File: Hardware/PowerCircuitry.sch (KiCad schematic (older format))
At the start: 32 parts, among them J4 Conn_01x02_Male, J5 Conn_01x02_Male, Q5 MMBT3904, Q6 MMBT3904, SW3 SW_SPST

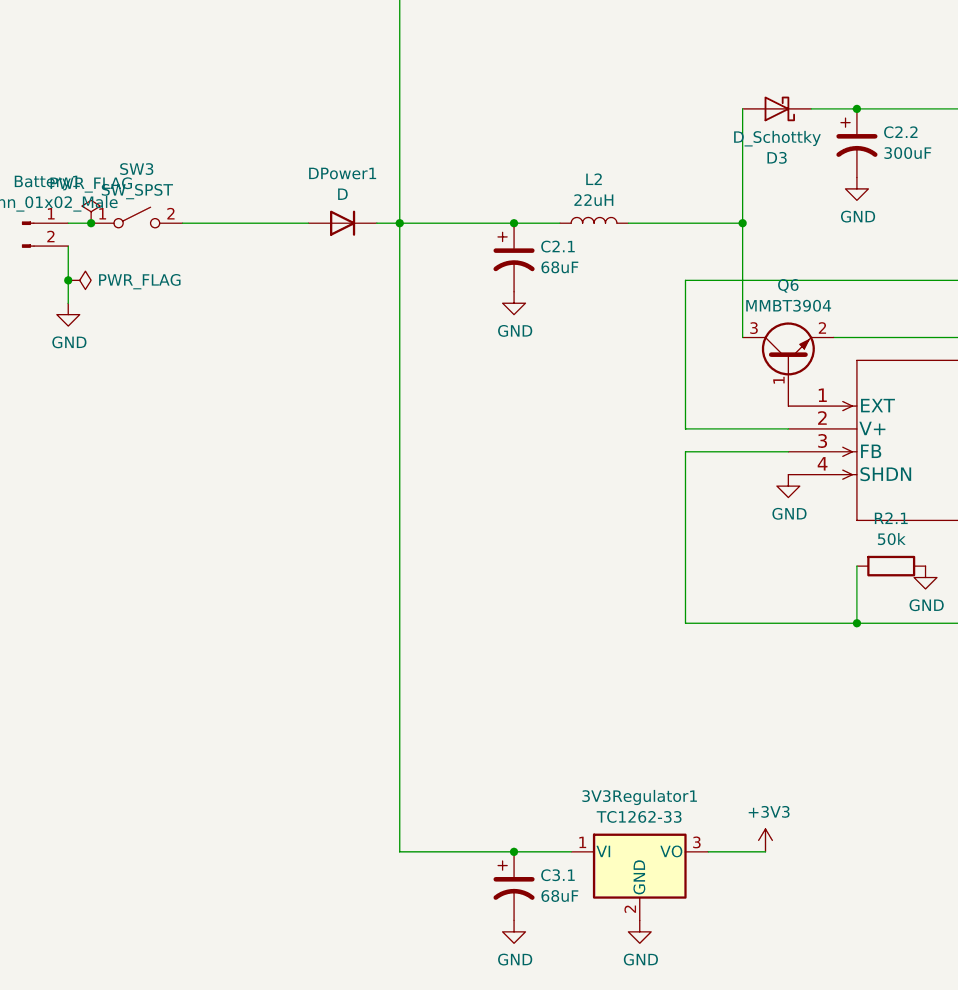
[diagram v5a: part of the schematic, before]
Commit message: Genuine Confusion
Changed to an ideal diode whatever tf that is
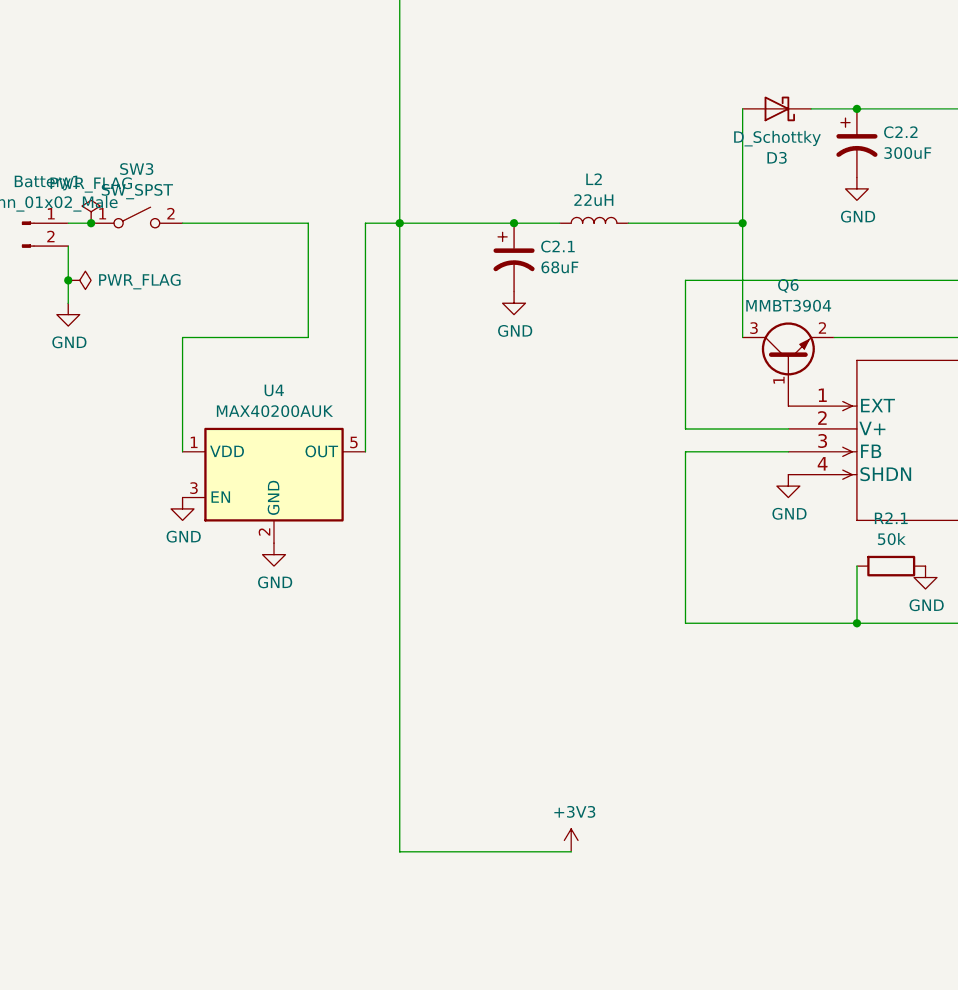
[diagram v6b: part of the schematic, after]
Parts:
- removed 3V3Regulator1: TC1262-33, Package_TO_SOT_SMD:SOT-223-3_TabPin2, symbol Regulator_Linear:TC1262-33
- removed C3.1: 68uF, Capacitor_SMD:C_0603_1608Metric, symbol Device:CP1
- removed DPower1: D, Diode_SMD:D_0603_1608Metric, symbol Device:D
- added U4: MAX40200AUK, Package_TO_SOT_SMD:SOT-23-5, symbol Analog_Switch:MAX40200AUK
- SW3: footprint Button_Switch_SMD:SW_DIP_SPSTx01_Slide_6.7x4.1mm_W6.73mm_P2.54mm_LowProfile_JPin -> Button_Switch_SMD:SW_DIP_SPSTx01_Slide_9.78x4.72mm_W8.61mm_P2.54mm
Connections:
- net +3V3: now also C1.1.1, C2.1.1, L1.1, L2.1, U4.5 (OUT)
- net GND: now also U4.2 (GND), U4.3 (EN)
- net at SW3.2 (B): now also U4.1 (VDD)
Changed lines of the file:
@@
 EESchema Schematic File Version 4
+LIBS:VLAD-cache
 EELAYER 30 0
 EELAYER END
@@
 	1000 4100 1000 4000
 $Comp
-L Regulator_Linear:TC1262-33 3V3Regulator1
-U 1 1 60725034
-P 3500 6500
-F 0 "3V3Regulator1" H 3500 6742 50  0000 C CNN
-F 1 "TC1262-33" H 3500 6651 50  0000 C CNN
-F 2 "Package_TO_SOT_SMD:SOT-223-3_TabPin2" H 3500 6725 50  0001 C CIN
-F 3 "http://ww1.microchip.com/downloads/en/DeviceDoc/21373C.pdf" H 3500 6200 50  0001 C CNN
-	1    3500 6500
-	1    0    0    -1
-$EndComp
-$Comp
 L power:+3V3 #PWR041
 U 1 1 6072852F
-P 4050 6500
-F 0 "#PWR041" H 4050 6350 50  0001 C CNN
-F 1 "+3V3" H 4065 6673 50  0000 C CNN
-F 2 "" H 4050 6500 50  0001 C CNN
-F 3 "" H 4050 6500 50  0001 C CNN
-	1    4050 6500
-	1    0    0    -1
-$EndComp
-$Comp
-L power:GND #PWR039
-U 1 1 60725C54
-P 3500 6800
-F 0 "#PWR039" H 3500 6550 50  0001 C CNN
-F 1 "GND" H 3505 6627 50  0000 C CNN
-F 2 "" H 3500 6800 50  0001 C CNN
-F 3 "" H 3500 6800 50  0001 C CNN
-	1    3500 6800
+P 3200 6500
+F 0 "#PWR041" H 3200 6350 50  0001 C CNN
+F 1 "+3V3" H 3215 6673 50  0000 C CNN
+F 2 "" H 3200 6500 50  0001 C CNN
+F 3 "" H 3200 6500 50  0001 C CNN
+	1    3200 6500
 	1    0    0    -1
 $EndComp
@@
 Wire Wire Line
 	4450 5500 3700 5500
-Wire Wire Line
-	3800 6500 4050 6500
 Connection ~ 2950 3750
 Wire Wire Line
@@
 	6550 5150 6950 5150
 Connection ~ 6950 5150
-Wire Wire Line
-	2350 3750 2450 3750
-$Comp
-L Device:CP1 C3.1
-U 1 1 607BC104
-P 2950 6650
-F 0 "C3.1" H 3065 6696 50  0000 L CNN
-F 1 "68uF" H 3065 6605 50  0000 L CNN
-F 2 "Capacitor_SMD:C_0603_1608Metric" H 2950 6650 50  0001 C CNN
-F 3 "~" H 2950 6650 50  0001 C CNN
-	1    2950 6650
-	1    0    0    -1
-$EndComp
-Wire Wire Line
-	2950 6500 3200 6500
-$Comp
-L power:GND #PWR038
-U 1 1 607BD21C
-P 2950 6800
-F 0 "#PWR038" H 2950 6550 50  0001 C CNN
-F 1 "GND" H 2955 6627 50  0000 C CNN
-F 2 "" H 2950 6800 50  0001 C CNN
-F 3 "" H 2950 6800 50  0001 C CNN
-	1    2950 6800
-	1    0    0    -1
-$EndComp
-Wire Wire Line
-	2450 6500 2950 6500
-Connection ~ 2950 6500
-$Comp
-L Device:D DPower1
-U 1 1 607B8542
-P 2200 3750
-F 0 "DPower1" H 2200 3534 50  0000 C CNN
-F 1 "D" H 2200 3625 50  0000 C CNN
-F 2 "Diode_SMD:D_0603_1608Metric" H 2200 3750 50  0001 C CNN
-F 3 "~" H 2200 3750 50  0001 C CNN
-	1    2200 3750
-	-1   0    0    1
-$EndComp
 $Comp
 L Connector:Conn_01x02_Male Battery1
@@
 	2450 1250 2450 3750
 $Comp
-L Switch:SW_SPST SW3
-U 1 1 608DCB23
-P 1300 3750
-F 0 "SW3" H 1300 3985 50  0000 C CNN
-F 1 "SW_SPST" H 1300 3894 50  0000 C CNN
-F 2 "Button_Switch_SMD:SW_DIP_SPSTx01_Slide_6.7x4.1mm_W6.73mm_P2.54mm_LowProfile_JPin" H 1300 3750 50  0001 C CNN
-F 3 "~" H 1300 3750 50  0001 C CNN
-	1    1300 3750
-	1    0    0    -1
-$EndComp
-Connection ~ 1100 3750
-$Comp
 L Mechanical:MountingHole_Pad H1
 U 1 1 6090A199
@@
 	1    0    0    -1
 $EndComp
+Wire Wire Line
+	2450 6500 3200 6500
+Connection ~ 1100 3750
+$Comp
+L Switch:SW_SPST SW3
+U 1 1 608DCB23
+P 1300 3750
+F 0 "SW3" H 1300 3985 50  0000 C CNN
+F 1 "SW_SPST" H 1300 3894 50  0000 C CNN
+F 2 "Button_Switch_SMD:SW_DIP_SPSTx01_Slide_9.78x4.72mm_W8.61mm_P2.54mm" H 1300 3750 50  0001 C CNN
+F 3 "~" H 1300 3750 50  0001 C CNN
+	1    1300 3750
+	1    0    0    -1
+$EndComp
+$Comp
+L Analog_Switch:MAX40200AUK U4
+U 1 1 60A1DB12
+P 1900 4850
+F 0 "U4" H 1900 5217 50  0000 C CNN
+F 1 "MAX40200AUK" H 1900 5126 50  0000 C CNN
+F 2 "Package_TO_SOT_SMD:SOT-23-5" H 1900 5350 50  0001 C CNN
+F 3 "https://datasheets.maximintegrated.com/en/ds/MAX40200.pdf" H 1900 5350 50  0001 C CNN
+	1    1900 4850
+	1    0    0    -1
+$EndComp
+Wire Wire Line
+	2050 3750 2050 4250
+Wire Wire Line
+	2050 4250 1500 4250
+Wire Wire Line
+	1500 4250 1500 4750
+Wire Wire Line
+	2300 4750 2300 3750
+Wire Wire Line
+	2300 3750 2450 3750
+$Comp
+L power:GND #PWR0101
+U 1 1 60A25E03
+P 1900 5150
+F 0 "#PWR0101" H 1900 4900 50  0001 C CNN
+F 1 "GND" H 1905 4977 50  0000 C CNN
+F 2 "" H 1900 5150 50  0001 C CNN
+F 3 "" H 1900 5150 50  0001 C CNN
+	1    1900 5150
+	1    0    0    -1
+$EndComp
+$Comp
+L power:GND #PWR0102
+U 1 1 60A2712E
+P 1500 4950
+F 0 "#PWR0102" H 1500 4700 50  0001 C CNN
+F 1 "GND" H 1505 4777 50  0000 C CNN
+F 2 "" H 1500 4950 50  0001 C CNN
+F 3 "" H 1500 4950 50  0001 C CNN
+	1    1500 4950
+	1    0    0    -1
+$EndComp

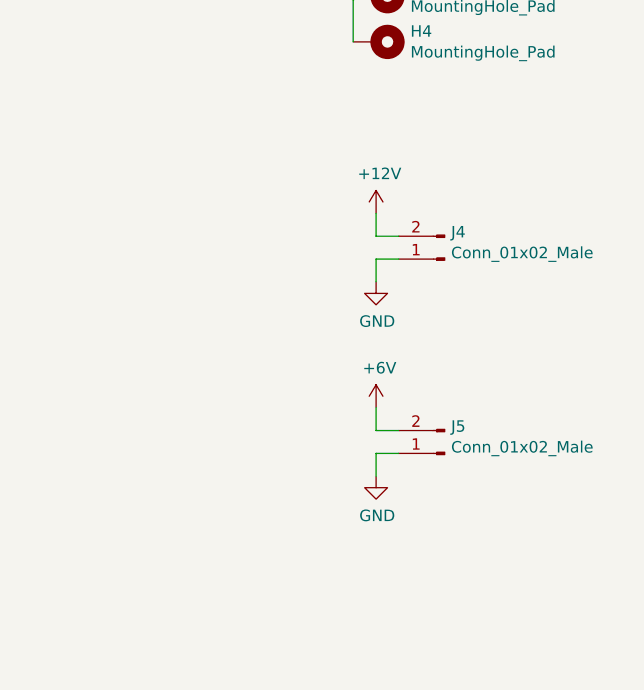
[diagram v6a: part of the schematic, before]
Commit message: Need to change pin headers for servo
Unsure at this stage, will look into which transistors etc to use.
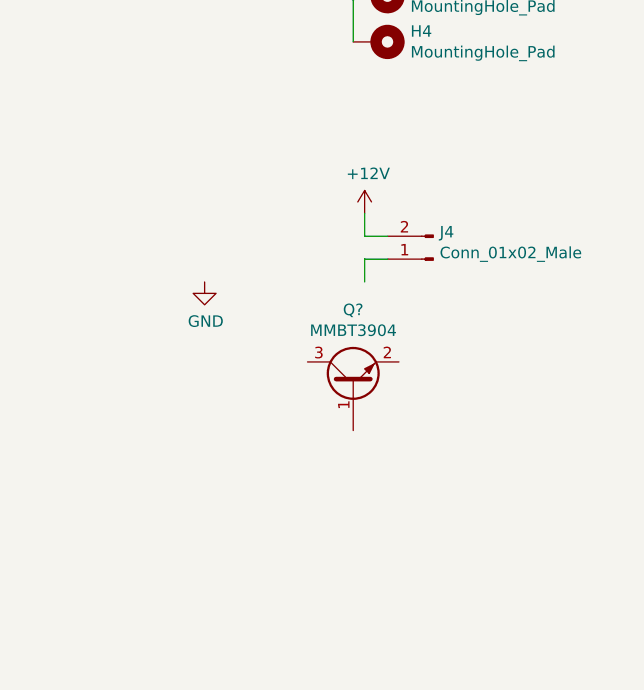
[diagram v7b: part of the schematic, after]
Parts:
- removed J5: Conn_01x02_Male, Connector_PinHeader_2.54mm:PinHeader_2x01_P2.54mm_Vertical, symbol Connector:Conn_01x02_Male
- added Q?: MMBT3904, Package_TO_SOT_SMD:SOT-23, symbol Transistor_BJT:MMBT3904
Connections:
- net GND: no longer J4.1 (Pin_1)
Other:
- moved on the sheet: J4
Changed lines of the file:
@@
 L Connector:Conn_01x02_Male J4
 U 1 1 609DE2A3
-P 9400 3000
-F 0 "J4" H 9372 2882 50  0000 R CNN
-F 1 "Conn_01x02_Male" H 9372 2973 50  0000 R CNN
-F 2 "Connector_PinHeader_2.54mm:PinHeader_2x01_P2.54mm_Vertical" H 9400 3000 50  0001 C CNN
-F 3 "~" H 9400 3000 50  0001 C CNN
-	1    9400 3000
+P 9350 3000
+F 0 "J4" H 9322 2882 50  0000 R CNN
+F 1 "Conn_01x02_Male" H 9322 2973 50  0000 R CNN
+F 2 "Connector_PinHeader_2.54mm:PinHeader_2x01_P2.54mm_Vertical" H 9350 3000 50  0001 C CNN
+F 3 "~" H 9350 3000 50  0001 C CNN
+	1    9350 3000
 	-1   0    0    1
 $EndComp
 Wire Wire Line
-	9200 2900 9100 2900
+	9150 2900 9050 2900
 Wire Wire Line
-	9200 3000 9100 3000
+	9150 3000 9050 3000
 Wire Wire Line
-	9100 3000 9100 3100
+	9050 3000 9050 3100
 Wire Wire Line
-	9100 2900 9100 2800
+	9050 2900 9050 2800
 $Comp
 L power:+12V #PWR054
 U 1 1 609E333D
-P 9100 2800
-F 0 "#PWR054" H 9100 2650 50  0001 C CNN
-F 1 "+12V" H 9115 2973 50  0000 C CNN
-F 2 "" H 9100 2800 50  0001 C CNN
-F 3 "" H 9100 2800 50  0001 C CNN
-	1    9100 2800
+P 9050 2800
+F 0 "#PWR054" H 9050 2650 50  0001 C CNN
+F 1 "+12V" H 9065 2973 50  0000 C CNN
+F 2 "" H 9050 2800 50  0001 C CNN
+F 3 "" H 9050 2800 50  0001 C CNN
+	1    9050 2800
 	1    0    0    -1
 $EndComp
@@
 L power:GND #PWR055
 U 1 1 609E5451
-P 9100 3100
-F 0 "#PWR055" H 9100 2850 50  0001 C CNN
-F 1 "GND" H 9105 2927 50  0000 C CNN
-F 2 "" H 9100 3100 50  0001 C CNN
-F 3 "" H 9100 3100 50  0001 C CNN
-	1    9100 3100
-	1    0    0    -1
-$EndComp
-$Comp
-L Connector:Conn_01x02_Male J5
-U 1 1 609E8D04
-P 9400 3850
-F 0 "J5" H 9372 3732 50  0000 R CNN
-F 1 "Conn_01x02_Male" H 9372 3823 50  0000 R CNN
-F 2 "Connector_PinHeader_2.54mm:PinHeader_2x01_P2.54mm_Vertical" H 9400 3850 50  0001 C CNN
-F 3 "~" H 9400 3850 50  0001 C CNN
-	1    9400 3850
-	-1   0    0    1
-$EndComp
-Wire Wire Line
-	9200 3750 9100 3750
-Wire Wire Line
-	9200 3850 9100 3850
-Wire Wire Line
-	9100 3850 9100 3950
-Wire Wire Line
-	9100 3750 9100 3650
-$Comp
-L power:GND #PWR057
-U 1 1 609E8D14
-P 9100 3950
-F 0 "#PWR057" H 9100 3700 50  0001 C CNN
-F 1 "GND" H 9105 3777 50  0000 C CNN
-F 2 "" H 9100 3950 50  0001 C CNN
-F 3 "" H 9100 3950 50  0001 C CNN
-	1    9100 3950
-	1    0    0    -1
-$EndComp
-$Comp
-L power:+6V #PWR056
-U 1 1 609EA9AA
-P 9100 3650
-F 0 "#PWR056" H 9100 3500 50  0001 C CNN
-F 1 "+6V" H 9115 3823 50  0000 C CNN
-F 2 "" H 9100 3650 50  0001 C CNN
-F 3 "" H 9100 3650 50  0001 C CNN
-	1    9100 3650
+P 8350 3100
+F 0 "#PWR055" H 8350 2850 50  0001 C CNN
+F 1 "GND" H 8355 2927 50  0000 C CNN
+F 2 "" H 8350 3100 50  0001 C CNN
+F 3 "" H 8350 3100 50  0001 C CNN
+	1    8350 3100
 	1    0    0    -1
 $EndComp
@@
 	1    0    0    -1
 $EndComp
+$Comp
+L Transistor_BJT:MMBT3904 Q?
+U 1 1 60A17A69
+P 9000 3550
+F 0 "Q?" V 9328 3550 50  0000 C CNN
+F 1 "MMBT3904" V 9237 3550 50  0000 C CNN
+F 2 "Package_TO_SOT_SMD:SOT-23" H 9200 3475 50  0001 L CIN
+F 3 "https://www.fairchildsemi.com/datasheets/2N/2N3904.pdf" H 9000 3550 50  0001 L CNN
+	1    9000 3550
+	0    -1   -1   0
+$EndComp
 $EndSCHEMATC

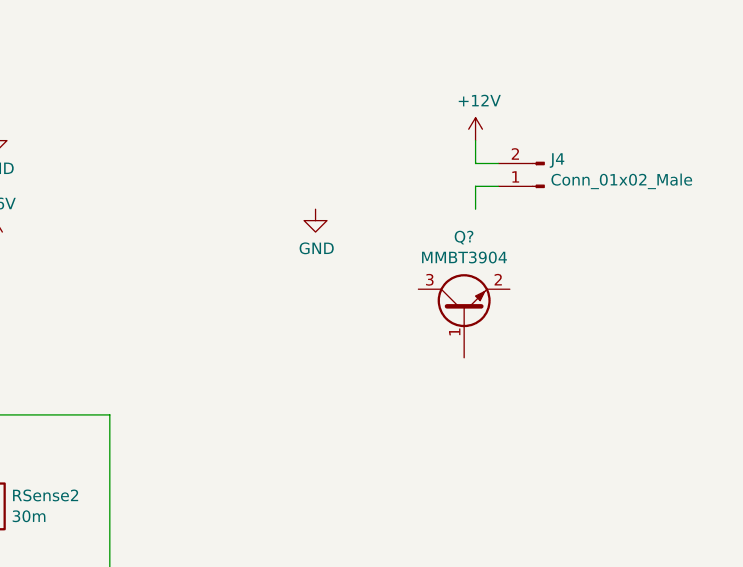
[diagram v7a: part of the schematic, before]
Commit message: Fixed minor issue with pin
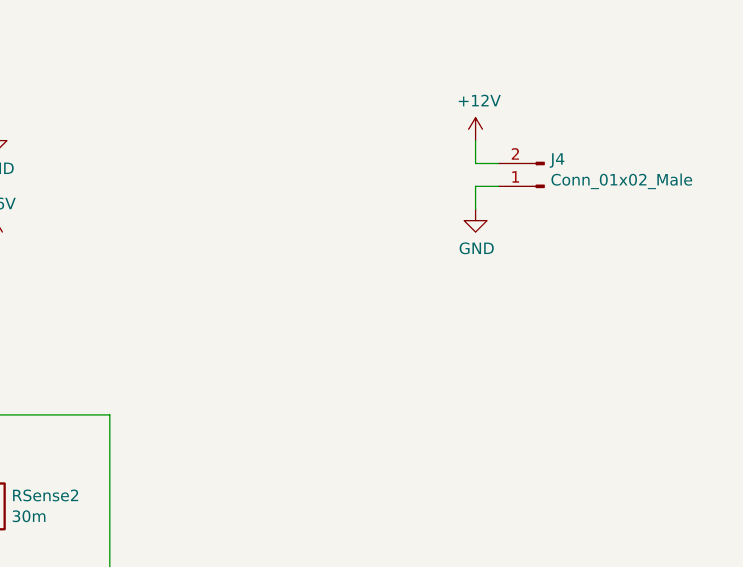
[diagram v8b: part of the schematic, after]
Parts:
- removed Q?: MMBT3904, Package_TO_SOT_SMD:SOT-23, symbol Transistor_BJT:MMBT3904
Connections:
- net GND: now also J4.1 (Pin_1)
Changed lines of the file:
@@
 L power:GND #PWR055
 U 1 1 609E5451
-P 8350 3100
-F 0 "#PWR055" H 8350 2850 50  0001 C CNN
-F 1 "GND" H 8355 2927 50  0000 C CNN
-F 2 "" H 8350 3100 50  0001 C CNN
-F 3 "" H 8350 3100 50  0001 C CNN
-	1    8350 3100
+P 9050 3100
+F 0 "#PWR055" H 9050 2850 50  0001 C CNN
+F 1 "GND" H 9055 2927 50  0000 C CNN
+F 2 "" H 9050 3100 50  0001 C CNN
+F 3 "" H 9050 3100 50  0001 C CNN
+	1    9050 3100
 	1    0    0    -1
 $EndComp
@@
 	1    0    0    -1
 $EndComp
-$Comp
-L Transistor_BJT:MMBT3904 Q?
-U 1 1 60A17A69
-P 9000 3550
-F 0 "Q?" V 9328 3550 50  0000 C CNN
-F 1 "MMBT3904" V 9237 3550 50  0000 C CNN
-F 2 "Package_TO_SOT_SMD:SOT-23" H 9200 3475 50  0001 L CIN
-F 3 "https://www.fairchildsemi.com/datasheets/2N/2N3904.pdf" H 9000 3550 50  0001 L CNN
-	1    9000 3550
-	0    -1   -1   0
-$EndComp
 $EndSCHEMATC
